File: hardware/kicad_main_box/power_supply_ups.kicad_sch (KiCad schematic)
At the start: 0 parts

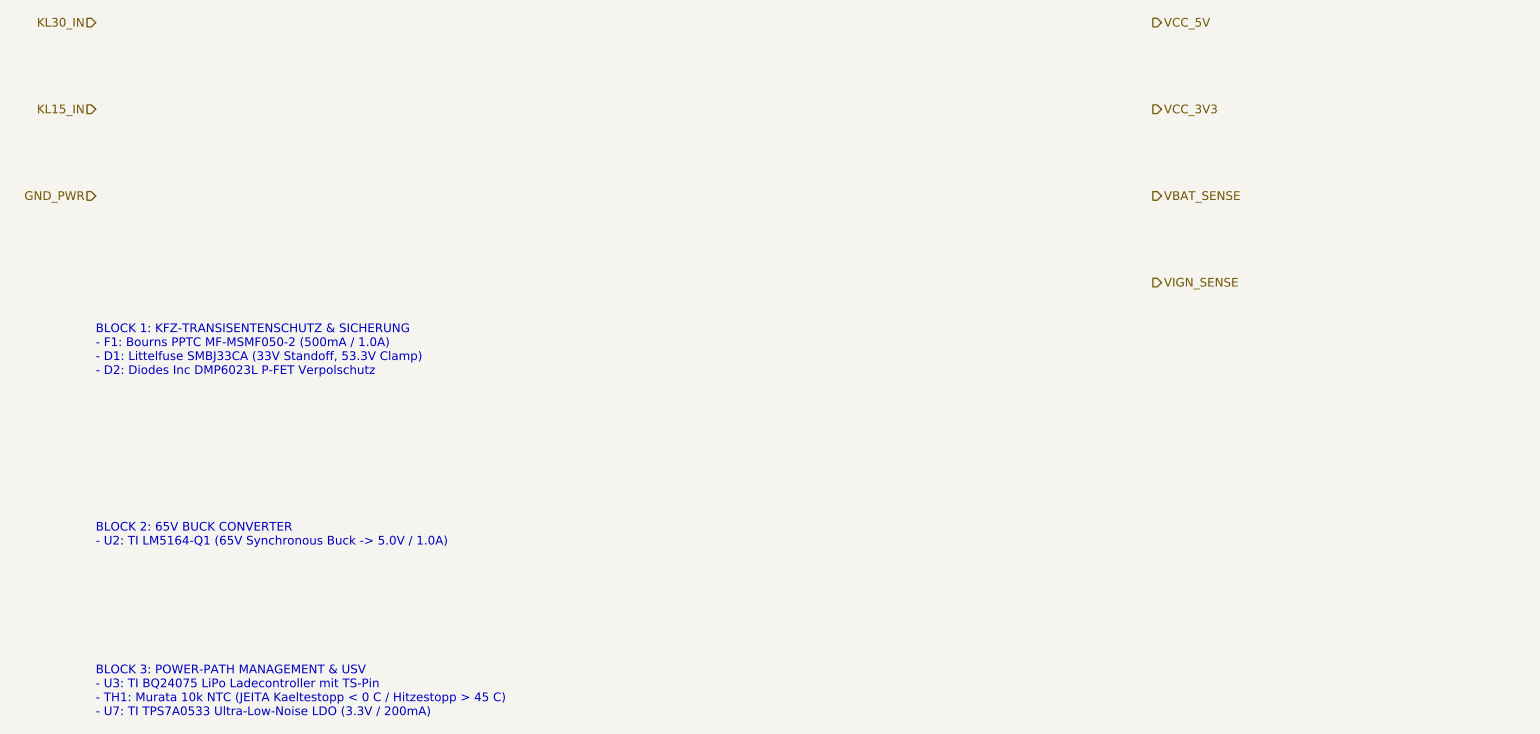
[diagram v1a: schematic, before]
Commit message: feat(kicad): Implement full graphical electronic schematic drawings (symbols, pins, wires, components) for all boards
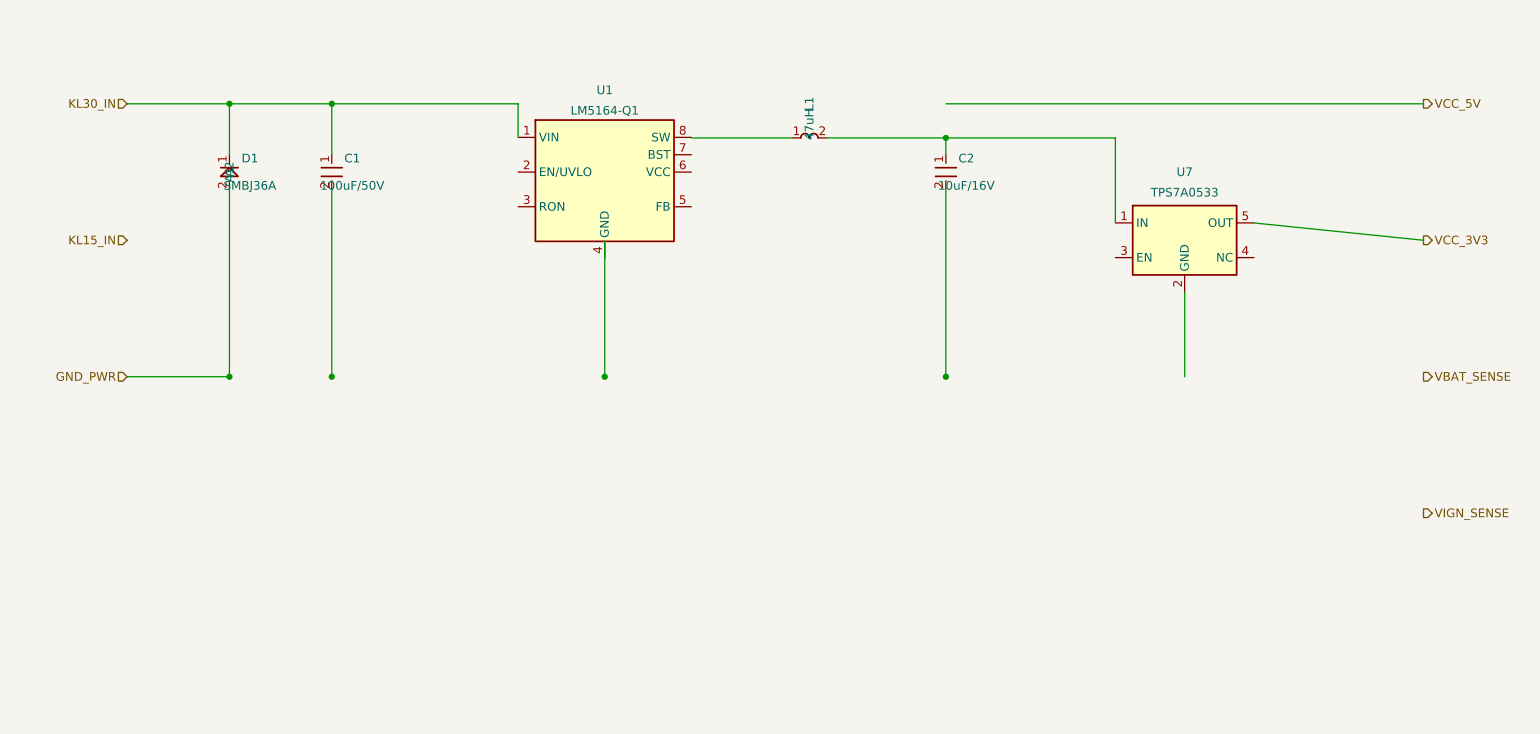
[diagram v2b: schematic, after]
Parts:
- added C1: 100uF/50V, symbol Device:C_Small
- added C2: 10uF/16V, symbol Device:C_Small
- added D1: SMBJ36A, symbol Device:D_TVS
- added L1: 47uH, symbol Device:L_Small
- added U1: LM5164-Q1, symbol Regulator_Switching:LM5164-Q1
- added U7: TPS7A0533, symbol Regulator_Linear:TPS7A0533
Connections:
- net GND_PWR: now also D1.2 (A2)
- net KL30_IN: now also C1.1, D1.1 (A1), U1.1 (VIN)
- net VCC_3V3: now also U7.5 (OUT)
- new net: C2.1, L1.2, U7.1 (IN)
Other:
- note removed: "BLOCK 1: KFZ-TRANSISENTENSCHUTZ & SICHERUNG - F1: Bourns PPTC MF-MSMF050-2 (500mA / 1.0A) - D1: Littelfuse SMBJ33CA (33V Standoff, 53.3V Clamp) - D2: Diodes Inc DMP6023L P-FET Verpolschutz"
- note removed: "BLOCK 2: 65V BUCK CONVERTER - U2: TI LM5164-Q1 (65V Synchronous Buck -> 5.0V / 1.0A)"
- note removed: "BLOCK 3: POWER-PATH MANAGEMENT & USV - U3: TI BQ24075 LiPo Ladecontroller mit TS-Pin - TH1: Murata 10k NTC (JEITA Kaeltestopp < 0 C / Hitzestopp > 45 C) - U7: TI TPS7A0533 Ultra-Low-Noise LDO (3.3V / 200mA)"
- company: (none) -> OpenMotorBridge Open Source Hardware
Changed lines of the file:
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@@
-(kicad_sch (version 20260206) (generator "eeschema") (generator_version "10.0")
-  (paper "A4")
-  (title_block
-    (title "OpenMotorBridge v8.0 - Stromversorgung & USV")
-    (date "2026-08-23")
-    (rev "v8.0")
-    (comment 1 "TI LM5164-Q1 (65V Buck) + TI BQ24075 (Power-Path & USV)")
-    (comment 2 "SMBJ33CA TVS + Bourns PPTC + Murata 10k NTC JEITA Kaelte-/Hitzeschutz")
-  )
-  (hierarchical_label "KL30_IN" (shape input) (at 25.4 38.1 180)
-    (effects (font (size 1.27 1.27)) (justify right))
-  )
-  (hierarchical_label "KL15_IN" (shape input) (at 25.4 50.8 180)
-    (effects (font (size 1.27 1.27)) (justify right))
-  )
-  (hierarchical_label "GND_PWR" (shape input) (at 25.4 63.5 180)
-    (effects (font (size 1.27 1.27)) (justify right))
-  )
-  (hierarchical_label "VCC_5V" (shape output) (at 180.34 38.1 0)
-    (effects (font (size 1.27 1.27)) (justify left))
-  )
-  (hierarchical_label "VCC_3V3" (shape output) (at 180.34 50.8 0)
-    (effects (font (size 1.27 1.27)) (justify left))
-  )
-  (hierarchical_label "VBAT_SENSE" (shape output) (at 180.34 63.5 0)
-    (effects (font (size 1.27 1.27)) (justify left))
-  )
-  (hierarchical_label "VIGN_SENSE" (shape output) (at 180.34 76.2 0)
-    (effects (font (size 1.27 1.27)) (justify left))
-  )
-  (text "BLOCK 1: KFZ-TRANSISENTENSCHUTZ & SICHERUNG\n- F1: Bourns PPTC MF-MSMF050-2 (500mA / 1.0A)\n- D1: Littelfuse SMBJ33CA (33V Standoff, 53.3V Clamp)\n- D2: Diodes Inc DMP6023L P-FET Verpolschutz" (at 25.4 90.0 0)
-    (effects (font (size 1.27 1.27)) (justify left bottom))
-  )
-  (text "BLOCK 2: 65V BUCK CONVERTER\n- U2: TI LM5164-Q1 (65V Synchronous Buck -> 5.0V / 1.0A)" (at 25.4 115.0 0)
-    (effects (font (size 1.27 1.27)) (justify left bottom))
-  )
-  (text "BLOCK 3: POWER-PATH MANAGEMENT & USV\n- U3: TI BQ24075 LiPo Ladecontroller mit TS-Pin\n- TH1: Murata 10k NTC (JEITA Kaeltestopp < 0 C / Hitzestopp > 45 C)\n- U7: TI TPS7A0533 Ultra-Low-Noise LDO (3.3V / 200mA)" (at 25.4 140.0 0)
-    (effects (font (size 1.27 1.27)) (justify left bottom))
-  )
+(kicad_sch
+	(version 20260206)
+	(generator "eeschema")
+	(generator_version "10.0")
+	(paper "A3")
+	(title_block
+		(title "OpenMotorBridge v8.0 - Stromversorgung & USV")
+		(date "2026-08-24")
+		(rev "v8.0")
+		(company "OpenMotorBridge Open Source Hardware")
+		(comment 1 "TI LM5164-Q1 (100V Buck) + TI BQ24075 (Power-Path & USV)")
+		(comment 2 "Automotive Transient Protection (ISO 7637-2, ISO 16750-2)")
+	)
+	;; =========================================================================
+	;; Hierarchical Labels
+	;; =========================================================================
+	(hierarchical_label "KL30_IN" (shape input) (at 30.0 50.0 180) (effects (font (size 1.27 1.27)) (justify right)))
+	(hierarchical_label "KL15_IN" (shape input) (at 30.0 70.0 180) (effects (font (size 1.27 1.27)) (justify right)))
+	(hierarchical_label "GND_PWR" (shape input) (at 30.0 90.0 180) (effects (font (size 1.27 1.27)) (justify right)))
+	(hierarchical_label "VCC_5V" (shape output) (at 220.0 50.0 0) (effects (font (size 1.27 1.27)) (justify left)))
+	(hierarchical_label "VCC_3V3" (shape output) (at 220.0 70.0 0) (effects (font (size 1.27 1.27)) (justify left)))
+	(hierarchical_label "VBAT_SENSE" (shape output) (at 220.0 90.0 0) (effects (font (size 1.27 1.27)) (justify left)))
+	(hierarchical_label "VIGN_SENSE" (shape output) (at 220.0 110.0 0) (effects (font (size 1.27 1.27)) (justify left)))
+	;; =========================================================================
+	;; Schematic Symbols Placement
+	;; =========================================================================
+	;; D1: Input TVS Diode
+	(symbol (lib_id "Device:D_TVS") (at 45.0 60.0 0) (unit 1)
+		(in_bom yes) (on_board yes) (dnp no)
+		(property "Reference" "D1" (at 48.0 58.0 0) (effects (font (size 1.27 1.27))))
+		(property "Value" "SMBJ36A" (at 48.0 62.0 0) (effects (font (size 1.27 1.27))))
+		(pin "1")
+		(pin "2")
+	)
+	;; C1: Input Electrolytic Cap (100uF 50V)
+	(symbol (lib_id "Device:C_Small") (at 60.0 60.0 0) (unit 1)
+		(in_bom yes) (on_board yes) (dnp no)
+		(property "Reference" "C1" (at 63.0 58.0 0) (effects (font (size 1.27 1.27))))
+		(property "Value" "100uF/50V" (at 63.0 62.0 0) (effects (font (size 1.27 1.27))))
+		(pin "1")
+		(pin "2")
+	)
+	;; U1: LM5164-Q1 Step-Down Converter
+	(symbol (lib_id "Regulator_Switching:LM5164-Q1") (at 100.0 60.0 0) (unit 1)
+		(in_bom yes) (on_board yes) (dnp no)
+		(property "Reference" "U1" (at 100.0 48.0 0) (effects (font (size 1.27 1.27))))
+		(property "Value" "LM5164-Q1" (at 100.0 51.0 0) (effects (font (size 1.27 1.27))))
+		(pin "1")
+		(pin "2")
+		(pin "3")
+		(pin "4")
+		(pin "5")
+		(pin "6")
+		(pin "7")
+		(pin "8")
+	)
+	;; L1: Buck Inductor 47uH
+	(symbol (lib_id "Device:L_Small") (at 130.0 55.0 90) (unit 1)
+		(in_bom yes) (on_board yes) (dnp no)
+		(property "Reference" "L1" (at 130.0 50.0 0) (effects (font (size 1.27 1.27))))
+		(property "Value" "47uH" (at 130.0 53.0 0) (effects (font (size 1.27 1.27))))
+		(pin "1")
+		(pin "2")
+	)
+	;; C2: Output Filter Cap (10uF 16V)
+	(symbol (lib_id "Device:C_Small") (at 150.0 60.0 0) (unit 1)
+		(in_bom yes) (on_board yes) (dnp no)
+		(property "Reference" "C2" (at 153.0 58.0 0) (effects (font (size 1.27 1.27))))
+		(property "Value" "10uF/16V" (at 153.0 62.0 0) (effects (font (size 1.27 1.27))))
+		(pin "1")
+		(pin "2")
+	)
+	;; U7: TPS7A0533 3.3V LDO
+	(symbol (lib_id "Regulator_Linear:TPS7A0533") (at 185.0 70.0 0) (unit 1)
+		(in_bom yes) (on_board yes) (dnp no)
+		(property "Reference" "U7" (at 185.0 60.0 0) (effects (font (size 1.27 1.27))))
+		(property "Value" "TPS7A0533" (at 185.0 63.0 0) (effects (font (size 1.27 1.27))))
+		(pin "1")
+		(pin "2")
+		(pin "3")
+		(pin "4")
+		(pin "5")
+	)
+	;; =========================================================================
+	;; Circuit Interconnecting Wires
+	;; =========================================================================
+	(wire (pts (xy 30.0 50.0) (xy 45.0 50.0)) (stroke (width 0) (type solid)))
+	(wire (pts (xy 45.0 50.0) (xy 45.0 57.46)) (stroke (width 0) (type solid)))
+	(wire (pts (xy 45.0 50.0) (xy 60.0 50.0)) (stroke (width 0) (type solid)))
+	(wire (pts (xy 60.0 50.0) (xy 60.0 57.46)) (stroke (width 0) (type solid)))
+	(wire (pts (xy 60.0 50.0) (xy 87.3 50.0)) (stroke (width 0) (type solid)))
+	(wire (pts (xy 87.3 50.0) (xy 87.3 54.92)) (stroke (width 0) (type solid)))
+	;; Inductor to SW pin
+	(wire (pts (xy 112.7 55.0) (xy 127.46 55.0)) (stroke (width 0) (type solid)))
+	;; Inductor to 5V Output
+	(wire (pts (xy 132.54 55.0) (xy 150.0 55.0)) (stroke (width 0) (type solid)))
+	(wire (pts (xy 150.0 55.0) (xy 150.0 57.46)) (stroke (width 0) (type solid)))
+	(wire (pts (xy 150.0 55.0) (xy 174.84 55.0)) (stroke (width 0) (type solid)))
+	(wire (pts (xy 174.84 55.0) (xy 174.84 67.46)) (stroke (width 0) (type solid)))
+	(wire (pts (xy 150.0 50.0) (xy 220.0 50.0)) (stroke (width 0) (type solid)))
+	;; LDO 3.3V Output
+	(wire (pts (xy 195.16 67.46) (xy 220.0 70.0)) (stroke (width 0) (type solid)))
+	;; Ground wire
+	(wire (pts (xy 30.0 90.0) (xy 45.0 90.0)) (stroke (width 0) (type solid)))
+	(wire (pts (xy 45.0 62.54) (xy 45.0 90.0)) (stroke (width 0) (type solid)))
+	(wire (pts (xy 60.0 62.54) (xy 60.0 90.0)) (stroke (width 0) (type solid)))
+	(wire (pts (xy 100.0 70.16) (xy 100.0 90.0)) (stroke (width 0) (type solid)))
+	(wire (pts (xy 150.0 62.54) (xy 150.0 90.0)) (stroke (width 0) (type solid)))
+	(wire (pts (xy 185.0 77.62) (xy 185.0 90.0)) (stroke (width 0) (type solid)))
+	;; Junctions
+	(junction (at 45.0 50.0) (diameter 0.9144) (color 0 0 0 0))
+	(junction (at 60.0 50.0) (diameter 0.9144) (color 0 0 0 0))
+	(junction (at 150.0 55.0) (diameter 0.9144) (color 0 0 0 0))
+	(junction (at 45.0 90.0) (diameter 0.9144) (color 0 0 0 0))
+	(junction (at 60.0 90.0) (diameter 0.9144) (color 0 0 0 0))
+	(junction (at 100.0 90.0) (diameter 0.9144) (color 0 0 0 0))
+	(junction (at 150.0 90.0) (diameter 0.9144) (color 0 0 0 0))
 )
